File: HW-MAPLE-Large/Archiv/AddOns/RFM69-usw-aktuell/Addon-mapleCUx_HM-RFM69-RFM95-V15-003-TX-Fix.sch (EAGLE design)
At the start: 37 parts, among them IC1 ATSHA204A, IC2 LD117ADT50TR, IC6 LM1117MPX-ADJ, U1 RFM69HCW, X4 1751248, X7 1751264

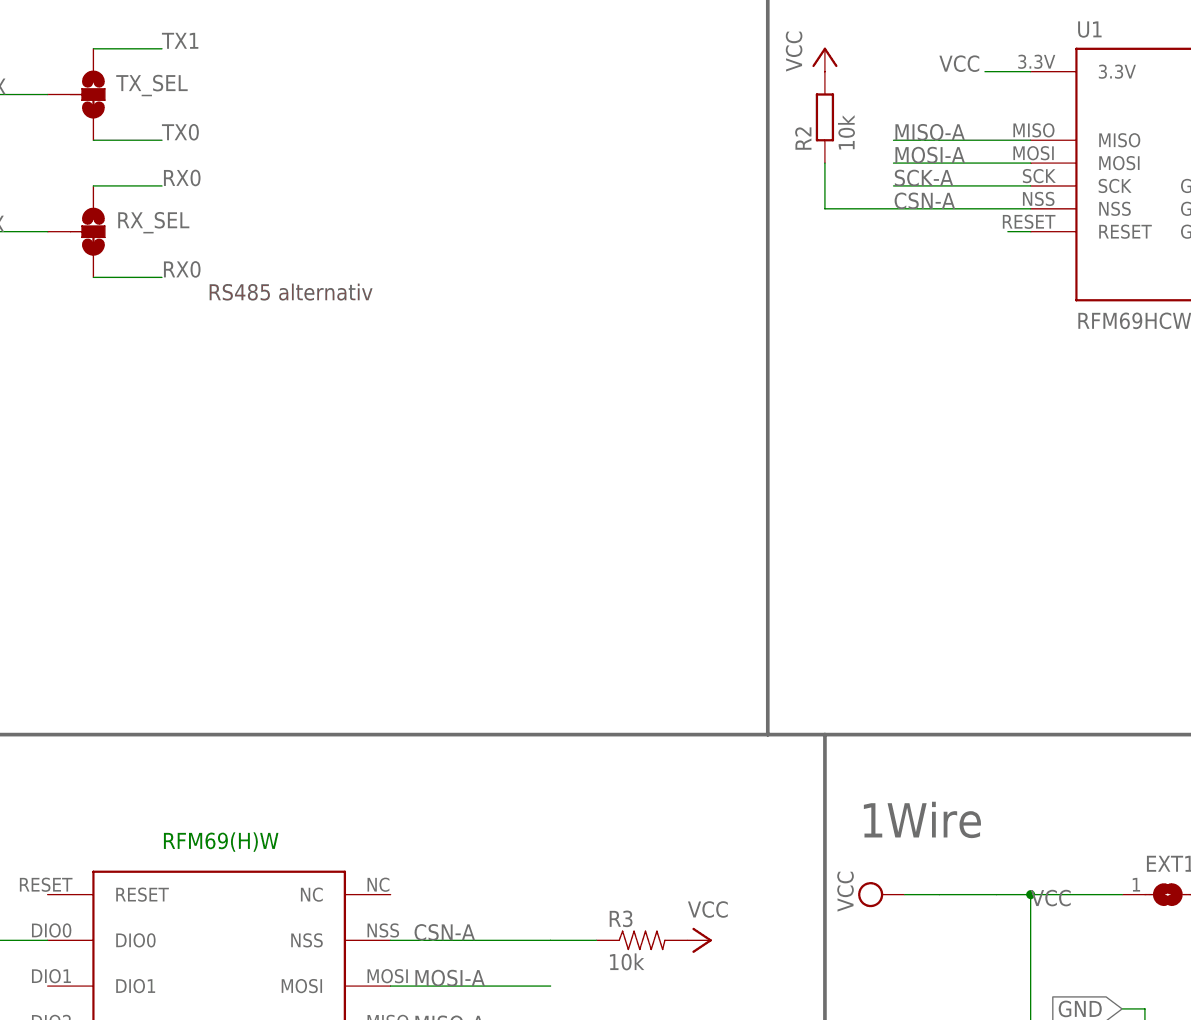
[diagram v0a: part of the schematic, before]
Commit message: Fix for old RFM69 AddOn + Docu
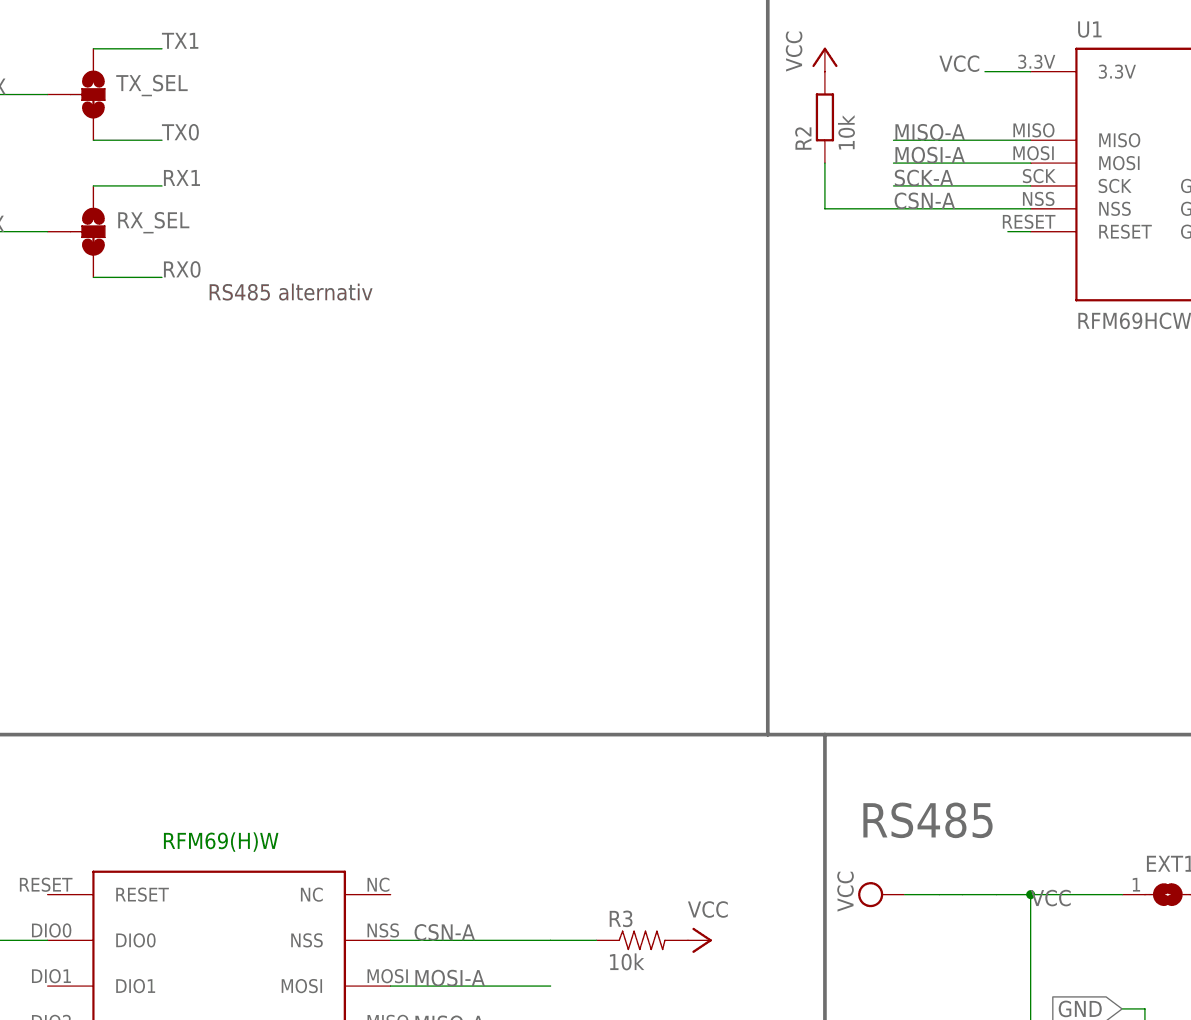
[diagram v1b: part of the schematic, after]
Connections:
- net RX0: no longer RX_SEL.1
- net RX1: now also RX_SEL.1
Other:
- note removed: "1Wire"
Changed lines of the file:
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@@
 <?xml version="1.0" encoding="utf-8"?>
 <!DOCTYPE eagle SYSTEM "eagle.dtd">
-<eagle version="9.2.2">
+<eagle version="9.3.0">
 <drawing>
 <settings>
@@
 Damit wird er Bus auf HIGH  gehalten wenn Teilnehmer passiv sind.
 AC-Widerstand ca. bei 120 Ohm (150 // (330+330)) = 122,2.</text>
-<text x="242.57" y="-194.31" size="3.81" layer="95" ratio="15">1Wire</text>
+<text x="242.57" y="-194.31" size="3.81" layer="95" ratio="15">RS485</text>
 <text x="364.49" y="-205.74" size="1.778" layer="95" rot="R90">External Power</text>
 <text x="142.24" y="-243.84" size="1.778" layer="97">Free Pins</text>
@@
 <label x="185.42" y="-71.12" size="1.778" layer="95"/>
 </segment>
+<segment>
+<pinref part="RX_SEL" gate="G$1" pin="1"/>
+<wire x1="157.48" y1="-121.92" x2="165.1" y2="-121.92" width="0.1524" layer="91"/>
+<label x="165.1" y="-121.92" size="1.778" layer="95"/>
+</segment>
 </net>
 <net name="TX1" class="0">
@@
 <net name="RX0" class="0">
 <segment>
-<pinref part="RX_SEL" gate="G$1" pin="1"/>
-<wire x1="157.48" y1="-121.92" x2="165.1" y2="-121.92" width="0.1524" layer="91"/>
-<label x="165.1" y="-121.92" size="1.778" layer="95"/>
-</segment>
-<segment>
 <wire x1="134.62" y1="-46.99" x2="142.24" y2="-46.99" width="0.1524" layer="91"/>
